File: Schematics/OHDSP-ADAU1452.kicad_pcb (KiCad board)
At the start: 4 copper layers, 100 x 100 mm, 294 parts, among them CN201 COAX, CN401 COAX, CN402 COAX, CN405 COAX, CN406 COAX, P201 CONN_2x1, P203 CONN_6X2, P204 CONN_6x1, P301 CONN_2x1, P302 CONN_2x1, P303 PIN, P304 PIN, P305 PIN, P306 PIN, P601 CONN_02X05, P602 CONN_02X05, P603 CONN_02X05, P604 CONN_02X05, P605 CONN_02X05, P606 CONN_6X2, P607 CONN_02X05, P608 CONN_02X05, P609 CONN_02X20, P610 CONN_02X05, P611 CONN_02X05, P612 CONN_02X05, P613 CONN_02X05, P614 CONN_02X05, P615 CONN_02X05, P616 CONN_02X05, SW202 SWITCH, U201 ADAU1452WBCPZ, U202 ADM13307-5ARZ, U203 25AA1024, U301 IC-REG-XRP7659ISTR-F, U302 IC-REG-XRP7659ISTR-F, U304 IC-REG-XC6210B332MR, U305 IC-REG-XC6210B332MR, U401 NB3L553, U501 IC-SPDIF-RX-OPTO, U502 IC-SPDIF-TX-OPTO, X201 24M576

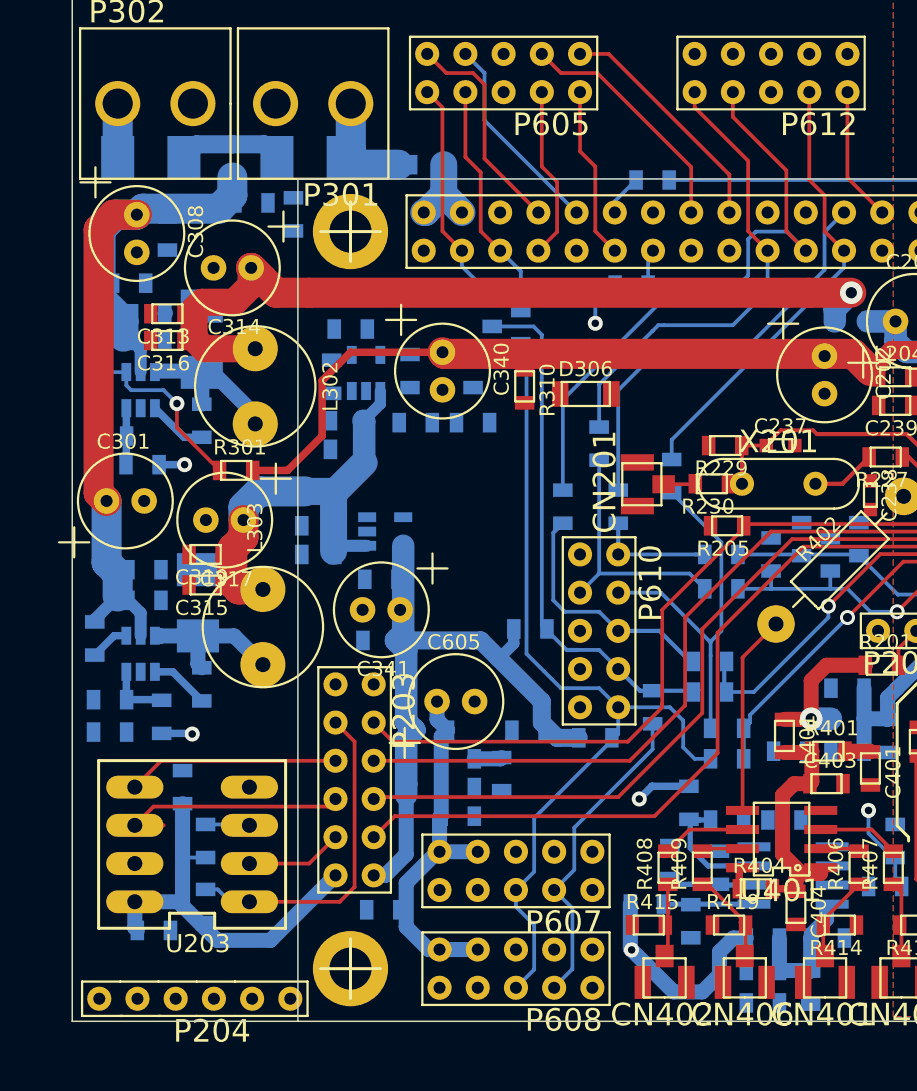
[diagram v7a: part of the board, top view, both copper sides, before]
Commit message: PCB work, Running Electrical Rule Check
PCB work, Running Electrical Rule Check:
Added no connects to schematics, added missing pull up on EEPROM, remove
USB_CLK/USB_RESET label on USB/I2C header and added NC. Minor change on
Pi connectors.
Removed old large PCB file.
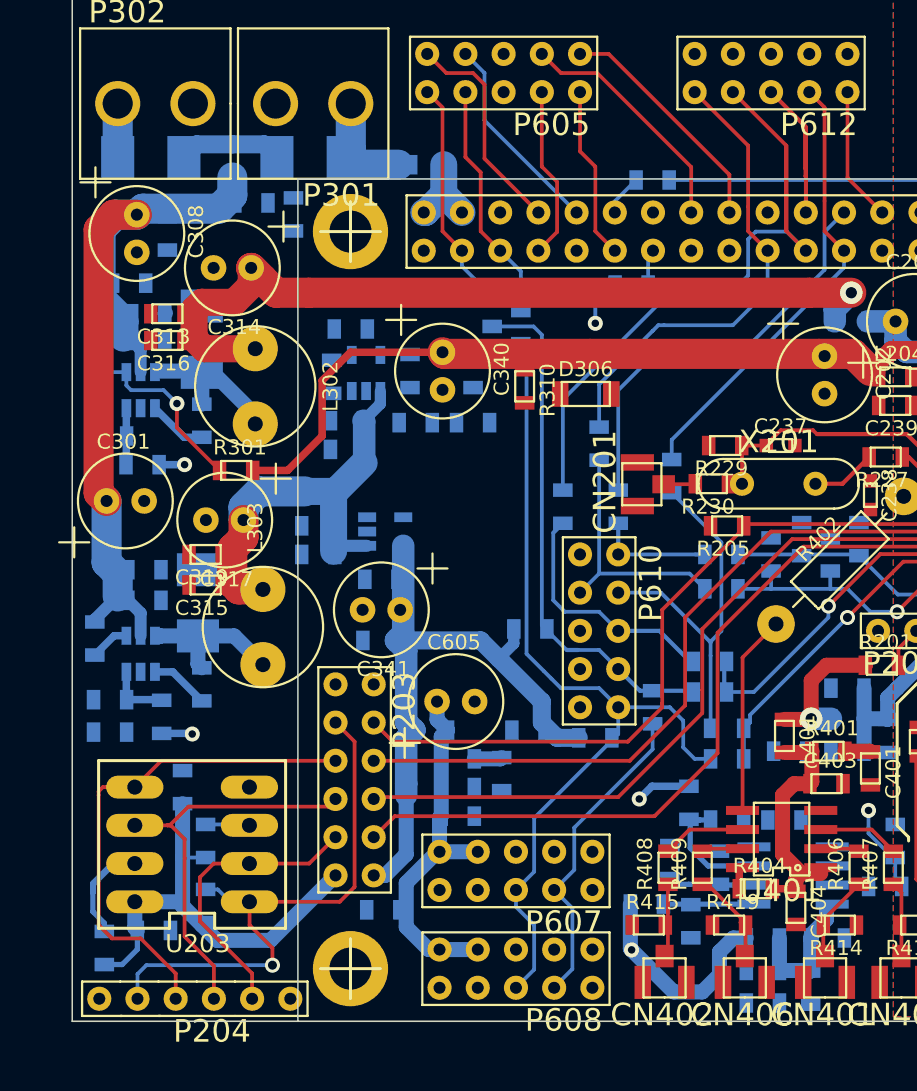
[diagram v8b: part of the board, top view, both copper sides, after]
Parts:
- added R235: 10k, OHDSP-Footprints-Pretty:SMD-0805, B.Cu at (207.1, 119.1)
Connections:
- net /Connectors/USB_CLK renamed Net-(P610-Pad2)
- net /Connectors/~USB_RESET renamed Net-(P610-Pad6)
- net Net-(C315-Pad1) renamed VCOM
- P605 pad 5: GNDD -> /Connectors/PI_GP4
- P605 pad 7: /Connectors/PI_GP4 -> /Connectors/PI_GP17
- P605 pad 9: /Connectors/PI_GP17 -> /Connectors/PI_GP22
- P609 pad 22: Net-(P609-Pad22) -> /Connectors/PI_GP25
- P612 pad 5: GNDD -> /Connectors/PI_GP25
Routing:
- net /ADAU1452/EE_SI: track 14.1 -> 35.5 mm
- net /Connectors/PI_GP25: track 0.00 -> 21.3 mm
- net /ADAU1452/EE_~CS: track 22.3 -> 38.0 mm, vias 0 -> 1
- net /ADAU1452/EE_SO: track 6.45 -> 19.6 mm
- net /ADAU1452/EE_SCK: track 16.0 -> 28.3 mm
- net Net-(R235-Pad2): track 0.00 -> 10.7 mm
- net /Connectors/PI_MISO: track 41.3 -> 47.0 mm
- net /Connectors/PI_GP4: track 11.5 -> 6.52 mm
- net /Connectors/PI_GP22: track 0.00 -> 3.94 mm
- net Net-(C252-Pad1): track 26.5 -> 30.4 mm
- net /Connectors/PI_GP17: track 11.5 -> 12.5 mm
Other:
- board text added: "Seeed Studio/Fusion PCB do a 1mm stackup that would give reasonable trace widths For 50ohm on top use inner top layer as ground (5mil thick) Trace width is 0.24mm, ground clearance anything <1mm For 75ohm on top use inner bottom layer as ground (29mil thick) Trace width is 0.5mm with ground on 0.5mm clearance For 100ohm on top use inner bottom layer as ground (29mil thick) Trace width is 0.25mm w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"
- board text removed: "Seeed Studio/Fusion PCB do a 1mm stackup that would give reasonable trace widths For 50ohm use inner layer as ground (5mil clearance), trace width is 0.24mm For 75ohm keep inner layers clear, bottom as ground, trace width is 0.5mm For 100ohm keep inner layers clear, bottom ground, use 0.25mm All are approximate..."
- board text removed: "This is the BCLK for the Pi - high speed.... Route carefully"
